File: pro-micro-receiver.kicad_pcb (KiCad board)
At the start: 4 copper layers, 63.7 x 19.5 mm, 58 parts, among them J1 USB_A_PLUG, J2 Conn_01x04, SW1 SW_Push, U1 TLV740P, U2 ATmega32U4-M, U3 YJ-14015, Y1 16MHz

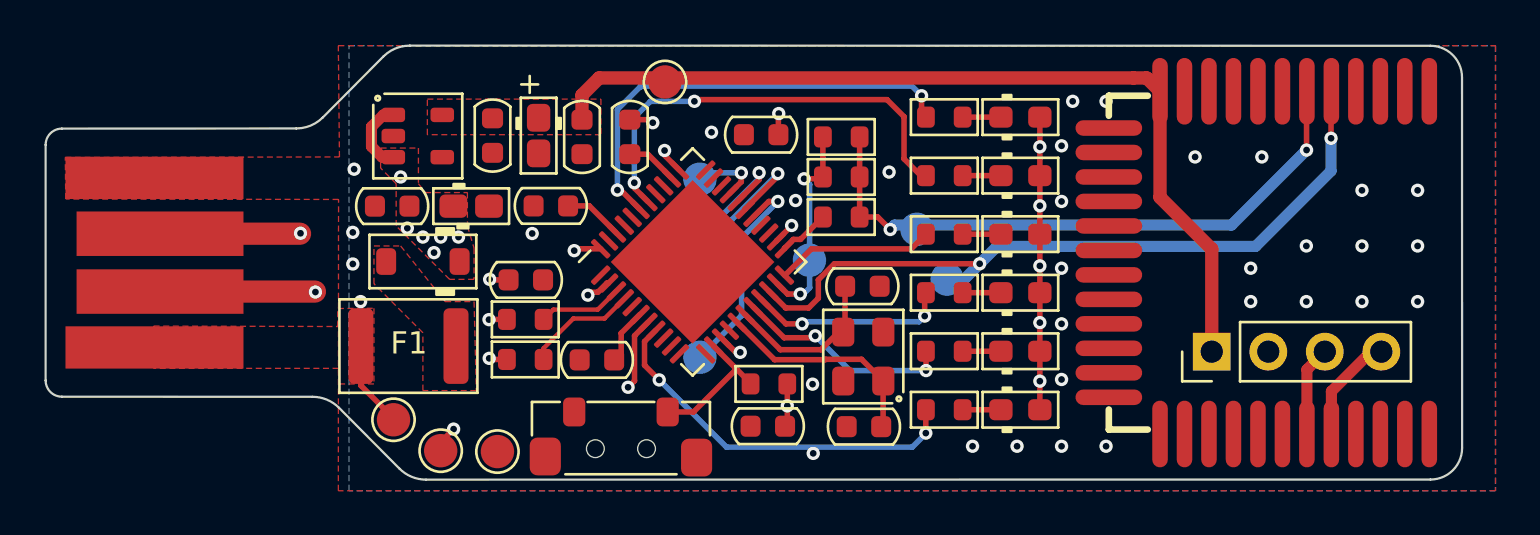
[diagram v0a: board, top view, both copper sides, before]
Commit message: Completed routing minified PCB
Passing DRC, tested gerbers on Aisler web
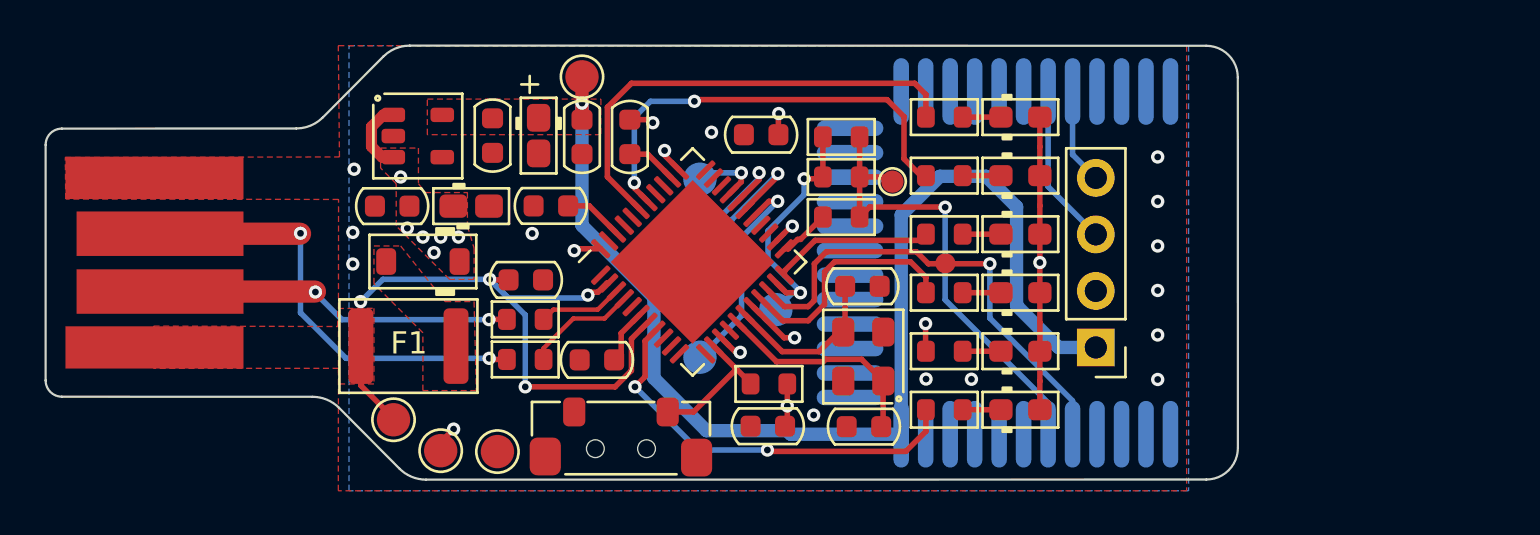
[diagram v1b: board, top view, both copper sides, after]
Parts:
- removed kibuzzard-63ACD5DB: G***, kibuzzard-63ACD5DB
- removed kibuzzard-63ACD5FF: G***, kibuzzard-63ACD5FF
- removed kibuzzard-63ACD615: G***, kibuzzard-63ACD615
- removed kibuzzard-63ACD627: G***, kibuzzard-63ACD627
- removed kibuzzard-63ACD667: G***, kibuzzard-63ACD667
- removed kibuzzard-63ACD680: G***, kibuzzard-63ACD680
- removed kibuzzard-63ACD69E: G***, kibuzzard-63ACD69E
- added kibuzzard-63AE0A2F: G***, kibuzzard-63AE0A2F, B.Cu at (86.0, 70.0)
- added kibuzzard-63AE0A69: G***, kibuzzard-63AE0A69, B.Cu at (86.0, 72.7)
- added kibuzzard-63AE0A7C: G***, kibuzzard-63AE0A7C, B.Cu at (86.0, 75.3)
- added kibuzzard-63AE0A8E: G***, kibuzzard-63AE0A8E, B.Cu at (86.0, 78.0)
- added kibuzzard-63AE0AB2: G***, kibuzzard-63AE0AB2, B.Cu at (93.6, 80.1)
- TP11, TP12: moved to F.Cu
- U3: moved to B.Cu
- moved U3 11.6 mm to (117.0, 73.8)
- moved J2 5.21 mm to (108.0, 77.6), turned to 180 degrees
- moved TP3 3.74 mm to (85.0, 65.4)
- moved TP13 2.68 mm to (93.7, 75.9)
- moved TP11 2.41 mm to (98.9, 70.1), turned to 0 degrees
- moved TP12 0.71 mm to (101.3, 73.8), turned to 0 degrees
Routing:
- net +3V3: track 40.3 -> 52.9 mm, vias 0 -> 1
- net RXI: track 34.0 -> 21.6 mm, vias 2 -> 1
- net TXODIV: track 28.0 -> 21.3 mm, vias 2 -> 1
- net SWDIO: track 4.03 -> 7.31 mm
- net TXO: track 9.49 -> 11.7 mm
- net /C_D2: track 8.97 -> 10.8 mm, vias 2 -> 0
- net UVCC: track 30.5 -> 31.8 mm
- net /TX_LED: track 17.3 -> 18.5 mm
- net /C_A3: track 20.3 -> 21.2 mm, vias 2 -> 0
- net SWCLK: track 4.90 -> 4.31 mm
- net GND: track 4.65 -> 4.64 mm, vias 32 -> 14
- net VCC: vias 19 -> 15
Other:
- board size 63.7 x 19.5 mm -> 53.6 x 19.5 mm
